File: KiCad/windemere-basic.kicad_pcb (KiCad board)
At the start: 2 copper layers, 152.4 x 158.8 mm, 67 parts, among them J3 Connector, J6 Barrel_Jack, SW1 Reset Button, U1 HD44780U, U2 WD65C02, U3 28C256, U4 62256, U5 WD65C22, U6 74HC00, U7 MM74C922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

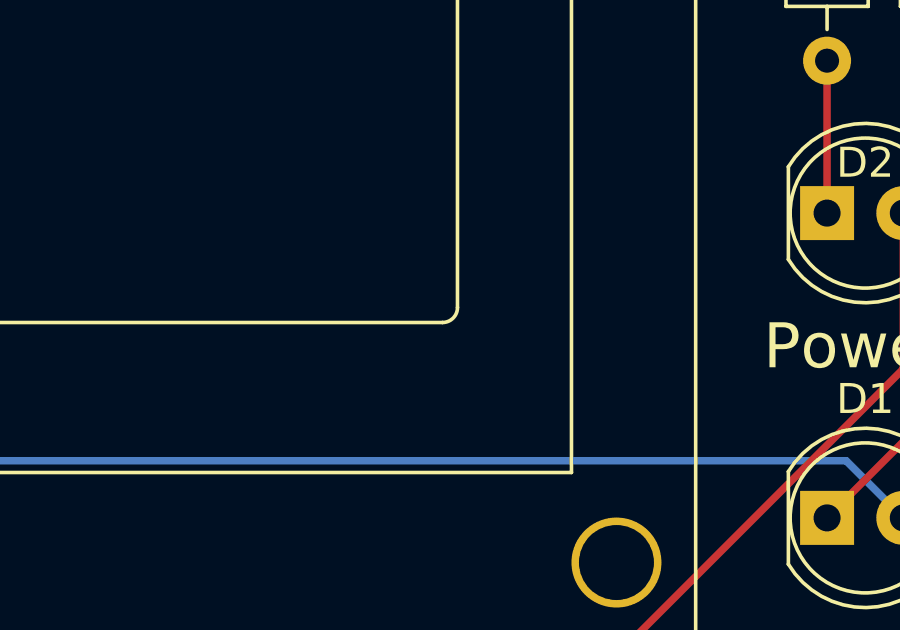
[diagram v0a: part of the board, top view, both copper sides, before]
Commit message: Remove unused text from front
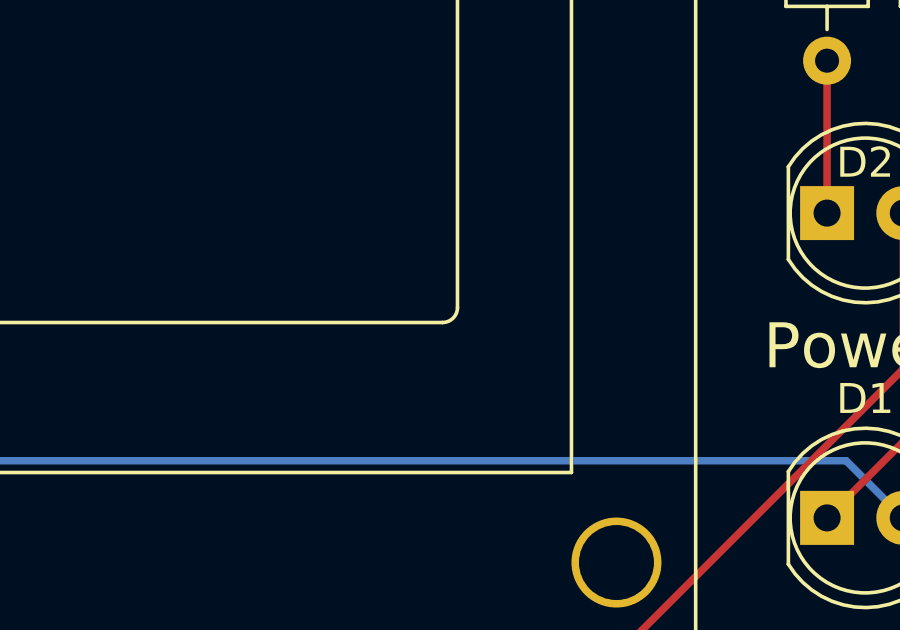
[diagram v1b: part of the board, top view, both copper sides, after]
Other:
- board text removed: "©2022 by Matt Rude <matt@mattrude.com>"
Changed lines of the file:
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@@
     (fp_arc (start 63.7 8) (mid 64.053553 8.146447) (end 64.2 8.5) (layer "F.SilkS") (width 0.12))
     (fp_arc (start 0.20066 22.9997) (mid -0.153162 22.853142) (end -0.29972 22.49932) (layer "F.SilkS") (width 0.12))
-    (fp_arc (start 64.20104 22.49932) (mid 64.054473 22.853115) (end 63.70066 22.9997) (layer "F.SilkS") (width 0.12))
+    (fp_arc (start 64.20104 22.49932) (mid 64.054479 22.85315) (end 63.70066 22.9997) (layer "F.SilkS") (width 0.12))
     (fp_line (start -8.25 33.75) (end 72.25 33.75) (layer "F.CrtYd") (width 0.05))
     (fp_line (start 72.25 -2.75) (end 72.25 33.75) (layer "F.CrtYd") (width 0.05))
@@
     (effects (font (size 1.5 1.5) (thickness 0.3)))
   )
-  (gr_text "©2022 by Matt Rude <matt@mattrude.com>" (at 233.675 188.575) (layer "F.Mask")
-    (effects (font (size 1 1) (thickness 0.15)))
-  )
   (dimension (type aligned) (layer "User.2")

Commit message: Moving to KiCad 7.0.5
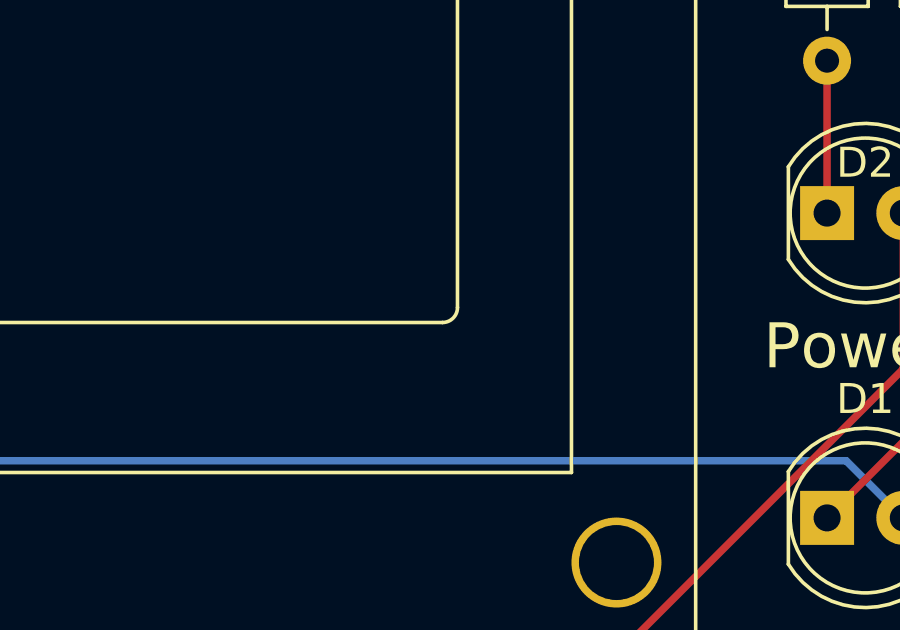
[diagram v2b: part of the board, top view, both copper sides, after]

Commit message: Update windemere-basic.kicad_pcb
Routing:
- net GND: track 93.5 -> 95.9 mm, vias 6 -> 8
- net +5V: track 527.2 -> 528.7 mm
- net Net-(J3-Pin_30): track 111.8 -> 110.8 mm
